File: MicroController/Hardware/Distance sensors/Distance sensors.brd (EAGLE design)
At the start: 87 x 40 mm, 37 parts, among them U1 LM2937IMP-5.0, U2 TXB0108PWR, U3 TLV1117-33CDCY, U4 TXB0108PWR, X1 0446200002, X2 0446200002, X3 0446200002

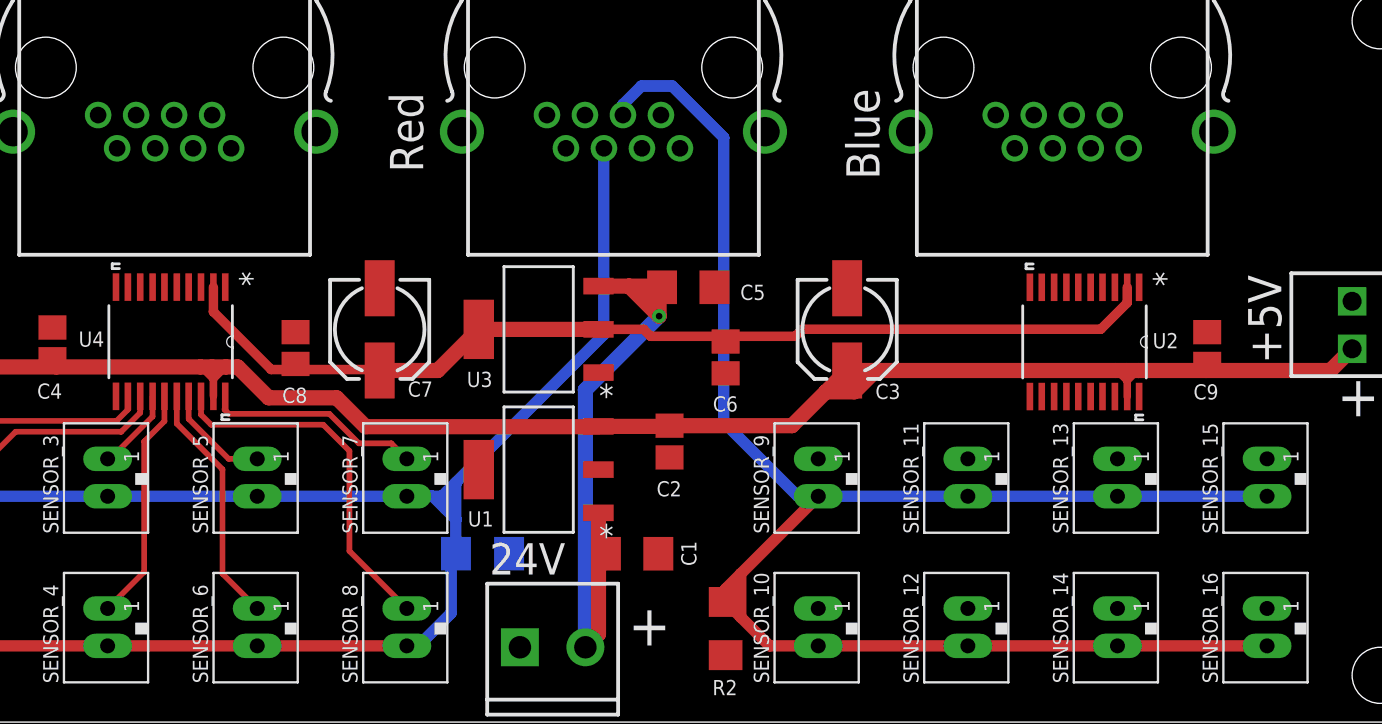
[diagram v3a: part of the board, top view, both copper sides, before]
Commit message: Version with two 5V terminals.
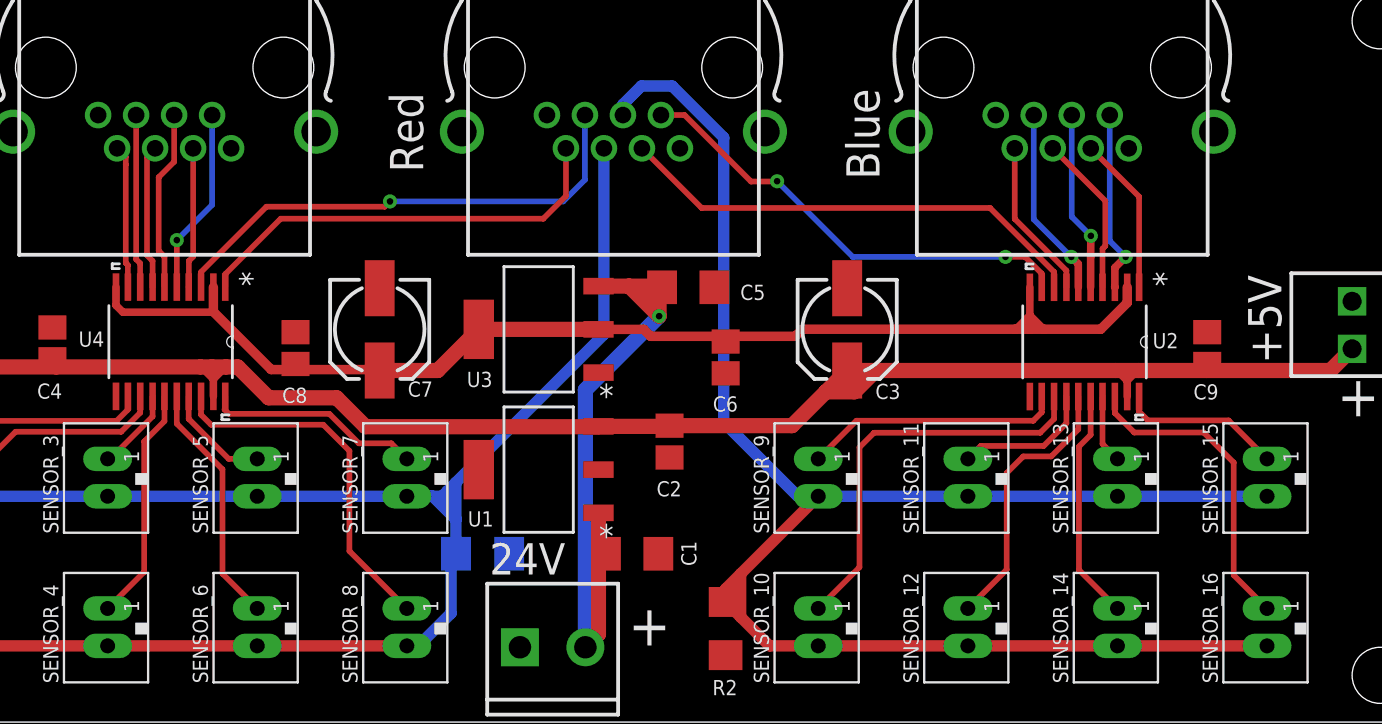
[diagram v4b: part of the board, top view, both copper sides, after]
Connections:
- removed net N$1: U4.1
- removed net N$2: U4.3
- removed net N$3: U4.4
- removed net N$4: U4.5
- removed net N$5: U4.6
- removed net N$6: U4.7
- removed net N$7: U4.8
- removed net N$8: U4.9
- net +3V3: now also U2.10, U4.10
- net ULTRA1: now also U4.9
- net ULTRA10: now also U2.8
- net ULTRA11: now also U2.7
- net ULTRA12: now also U2.6
- net ULTRA13: now also U2.4
- net ULTRA14: now also U2.5
- net ULTRA15: now also U2.1
- net ULTRA16: now also U2.3
- net ULTRA2: now also U4.8
- net ULTRA3: now also U4.7
- net ULTRA4: now also U4.6
- net ULTRA5: now also U4.4
- net ULTRA6: now also U4.5
- net ULTRA7: now also U4.1
- net ULTRA8: now also U4.3
- net ULTRA9: now also U2.9
- net ULTRAS10: now also U2.13
- net ULTRAS11: now also U2.14
- net ULTRAS12: now also U2.15
- net ULTRAS13: now also U2.17
- net ULTRAS14: now also U2.16
- net ULTRAS15: now also U2.20
- net ULTRAS16: now also U2.18
- net ULTRAS9: now also U2.12
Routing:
- net ULTRA8: track 0.00 -> 26.8 mm, vias 0 -> 1
- net ULTRA10: track 0.00 -> 25.6 mm
- net ULTRA9: track 0.00 -> 24.6 mm, vias 0 -> 2
- net ULTRA7: track 0.00 -> 23.2 mm
- net ULTRAS10: track 0.00 -> 21.8 mm
- net ULTRAS16: track 0.00 -> 16.9 mm
- net ULTRAS12: track 0.00 -> 14.7 mm
- net ULTRAS9: track 0.00 -> 13.8 mm
- net ULTRAS14: track 0.00 -> 12.4 mm
- net +3V3: track 54.9 -> 65.6 mm
- net ULTRA12: track 0.00 -> 10.2 mm, vias 0 -> 1
- net ULTRA6: track 0.00 -> 9.98 mm, vias 0 -> 1
- net ULTRA16: track 0.00 -> 9.82 mm, vias 0 -> 1
- net ULTRA4: track 0.00 -> 9.67 mm
- net ULTRA14: track 0.00 -> 9.63 mm, vias 0 -> 1
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
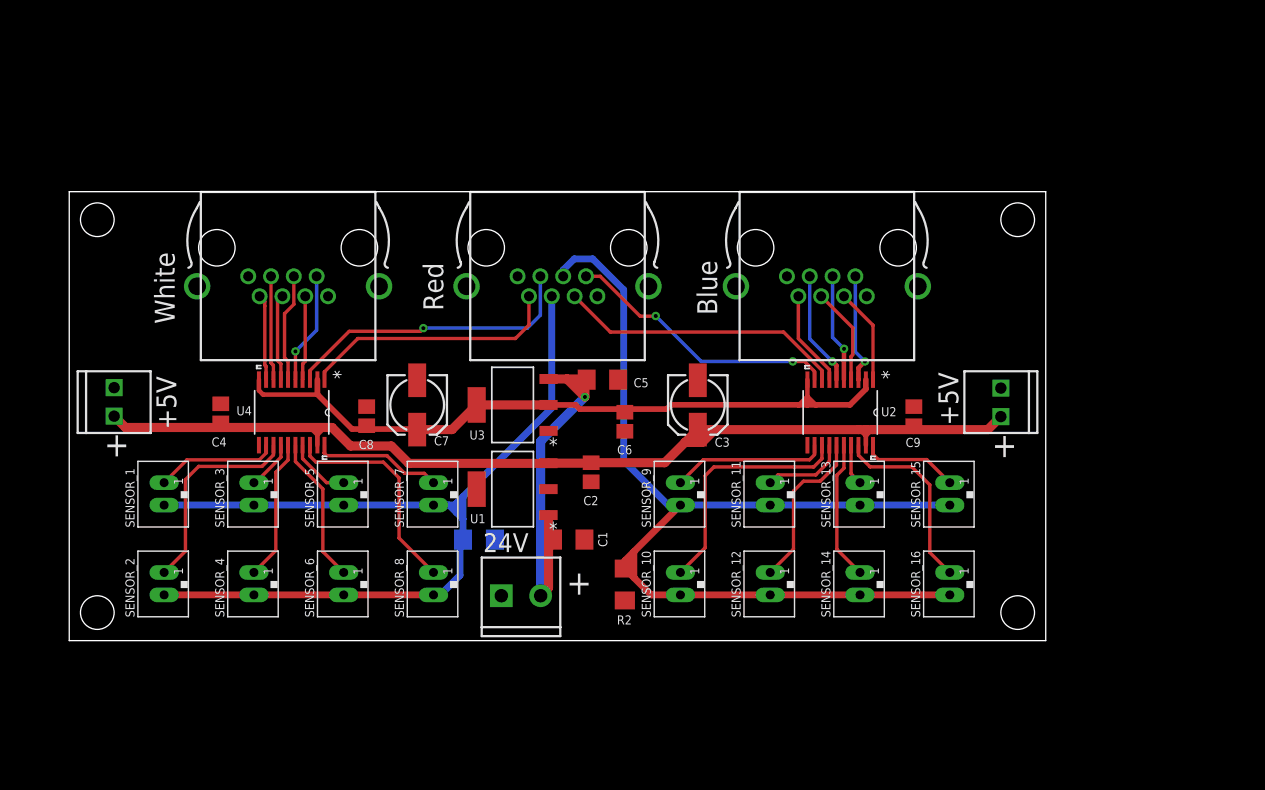
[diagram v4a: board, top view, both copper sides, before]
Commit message: Changed to one 4-pin connector for each sensor.
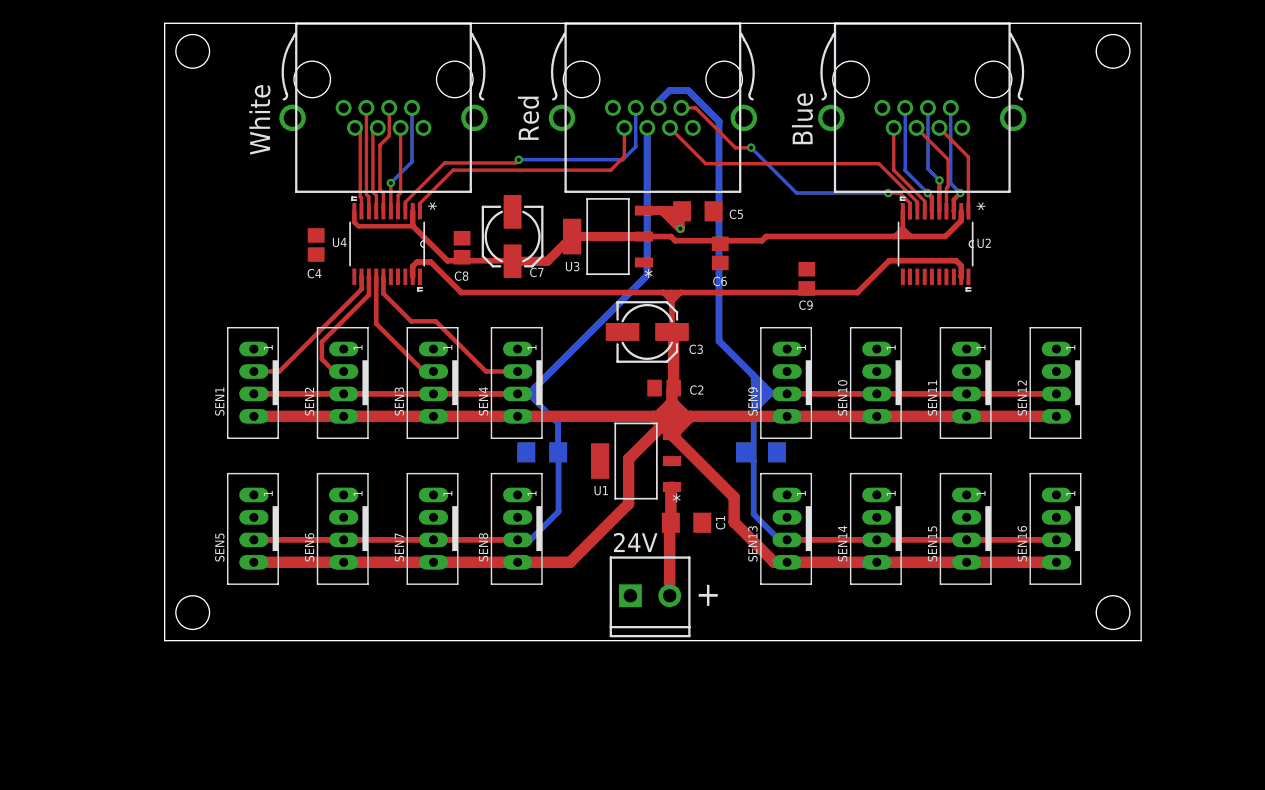
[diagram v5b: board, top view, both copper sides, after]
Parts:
- removed 5V, J1: (no value), SparkFun-Connectors:1X02_2.54_SCREWTERM
- removed SENSOR_1, SENSOR_10, SENSOR_11, SENSOR_12, SENSOR_13, SENSOR_14, SENSOR_15, SENSOR_16, SENSOR_2, SENSOR_3, SENSOR_4, SENSOR_5, SENSOR_6, SENSOR_7, SENSOR_8, SENSOR_9: JST-PH_2-PIN_HEADER, SRG:JST_B2B-PH_HEADER
- added SEN1, SEN10, SEN11, SEN12, SEN13, SEN14, SEN15, SEN16, SEN2, SEN3, SEN4, SEN5, SEN6, SEN7, SEN8, SEN9: JST-PH_4-PIN_HEADER, SRG:JST_B4B-PH_HEADER
- moved C4 17.2 mm to (13.5, 35.2)
- moved C5 17.2 mm to (47.5, 38.2)
- moved C6 17.2 mm to (49.5, 34.5)
- moved C7 17.2 mm to (31.0, 36.0)
- moved C8 17.2 mm to (26.5, 35.0)
- moved U3 17.2 mm to (39.5, 36.0)
- moved X1 17.2 mm to (19.5, 50.0)
- moved X2 17.2 mm to (43.5, 50.0)
- moved X3 17.2 mm to (67.5, 50.0)
- moved U2 17.2 mm to (68.7, 35.3)
- moved U4 17.2 mm to (19.8, 35.3)
- moved R2 16.9 mm to (53.1, 16.8), flipped to the bottom, turned to 0 degrees
- moved C9 15.5 mm to (57.2, 32.2)
- moved 24V 11.5 mm to (41.5, 4.00)
- moved U1 11.3 mm to (42.0, 16.0)
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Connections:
- net +5V: now also SEN1.P4, SEN10.P4, SEN11.P4, SEN12.P4, SEN13.P4, SEN14.P4, SEN15.P4, SEN16.P4, SEN2.P4, SEN3.P4, SEN4.P4, SEN5.P4, SEN6.P4, SEN7.P4, SEN8.P4, SEN9.P4; no longer 5V.P2, J1.P1
- net GND: now also SEN1.P1, SEN10.P1, SEN11.P1, SEN12.P1, SEN13.P1, SEN14.P1, SEN15.P1, SEN16.P1, SEN2.P1, SEN3.P1, SEN4.P1, SEN5.P1, SEN6.P1, SEN7.P1, SEN8.P1, SEN9.P1; no longer 5V.P1, J1.P2
- net TRIGGER_1: now also SEN1.P3, SEN2.P3, SEN3.P3, SEN4.P3, SEN5.P3, SEN6.P3, SEN7.P3, SEN8.P3; no longer SENSOR_1.P2, SENSOR_2.P2, SENSOR_3.P2, SENSOR_4.P2, SENSOR_5.P2, SENSOR_6.P2, SENSOR_7.P2, SENSOR_8.P2
- net TRIGGER_2: now also SEN10.P3, SEN11.P3, SEN12.P3, SEN13.P3, SEN14.P3, SEN15.P3, SEN16.P3, SEN9.P3; no longer SENSOR_10.P2, SENSOR_11.P2, SENSOR_12.P2, SENSOR_13.P2, SENSOR_14.P2, SENSOR_15.P2, SENSOR_16.P2, SENSOR_9.P2
- net ULTRAS1: now also SEN1.P2; no longer SENSOR_1.P1
- net ULTRAS10: now also SEN10.P2; no longer SENSOR_10.P1
- net ULTRAS11: now also SEN11.P2; no longer SENSOR_11.P1
- net ULTRAS12: now also SEN12.P2; no longer SENSOR_12.P1
- net ULTRAS13: now also SEN13.P2; no longer SENSOR_13.P1
- net ULTRAS14: now also SEN14.P2; no longer SENSOR_14.P1
- net ULTRAS15: now also SEN15.P2; no longer SENSOR_15.P1
- net ULTRAS16: now also SEN16.P2; no longer SENSOR_16.P1
- net ULTRAS2: now also SEN2.P2; no longer SENSOR_2.P1
- net ULTRAS3: now also SEN3.P2; no longer SENSOR_3.P1
- net ULTRAS4: now also SEN4.P2; no longer SENSOR_4.P1
- net ULTRAS5: now also SEN5.P2; no longer SENSOR_5.P1
- net ULTRAS6: now also SEN6.P2; no longer SENSOR_6.P1
- net ULTRAS7: now also SEN7.P2; no longer SENSOR_7.P1
- net ULTRAS8: now also SEN8.P2; no longer SENSOR_8.P1
- net ULTRAS9: now also SEN9.P2; no longer SENSOR_9.P1
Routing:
- net +5V: track 93.1 -> 232.6 mm
- net ULTRAS10: track 21.8 -> 0.00 mm
- net ULTRAS8: track 19.4 -> 0.00 mm
- net +24V: track 34.7 -> 17.1 mm
- net ULTRAS16: track 16.9 -> 0.00 mm
- net ULTRAS12: track 14.7 -> 0.00 mm
- net ULTRAS9: track 13.8 -> 0.00 mm
- net TRIGGER_2: track 93.4 -> 106.9 mm
- net ULTRAS6: track 13.1 -> 0.00 mm
- net ULTRAS14: track 12.4 -> 0.00 mm
- net ULTRAS7: track 11.6 -> 0.00 mm
- net ULTRAS15: track 8.69 -> 0.00 mm
- net ULTRAS11: track 7.49 -> 0.00 mm
- net ULTRAS2: track 18.7 -> 11.5 mm
- net TRIGGER_1: track 86.4 -> 93.4 mm
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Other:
- board size 87 x 40 mm -> 87 x 55 mm
- board text removed: "+5V"

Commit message: Finished the first version of the Ultrasone PCB.
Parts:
- added C10, C11, C12, C13: (no value), adafruit:C0805
- moved C4 24.2 mm to (37.1, 29.8), turned to 270 degrees
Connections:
- net +5V: now also C10.1, C11.1, C12.1, C13.1
- net GND: now also C10.2, C11.2, C12.2, C13.2
- net ULTRA13: now also U2.5; no longer U2.4
- net ULTRA14: now also U2.4; no longer U2.5
- net ULTRA15: now also U2.3; no longer U2.1
- net ULTRA16: now also U2.1; no longer U2.3
- net ULTRA5: now also U4.5; no longer U4.4
- net ULTRA6: now also U4.4; no longer U4.5
- net ULTRA7: now also U4.3; no longer U4.1
- net ULTRA8: now also U4.1; no longer U4.3
- net ULTRAS13: now also U2.16; no longer U2.17
- net ULTRAS14: now also U2.17; no longer U2.16
- net ULTRAS15: now also U2.18; no longer U2.20
- net ULTRAS16: now also U2.20; no longer U2.18
- net ULTRAS5: now also U4.16; no longer U4.17
- net ULTRAS6: now also U4.17; no longer U4.16
- net ULTRAS7: now also U4.18; no longer U4.20
- net ULTRAS8: now also U4.20; no longer U4.18
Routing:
- net +24V: track 17.1 -> 50.2 mm
- net ULTRAS13: track 0.00 -> 28.9 mm, vias 0 -> 1
- net ULTRAS5: track 0.00 -> 28.0 mm, vias 0 -> 1
- net ULTRAS8: track 0.00 -> 26.2 mm, vias 0 -> 1
- net ULTRAS16: track 0.00 -> 25.8 mm, vias 0 -> 1
- net ULTRAS7: track 0.00 -> 25.7 mm, vias 0 -> 1
- net ULTRAS15: track 0.00 -> 25.4 mm, vias 0 -> 1
- net ULTRAS6: track 0.00 -> 25.0 mm, vias 0 -> 1
- net ULTRAS14: track 0.00 -> 24.9 mm, vias 0 -> 1
- net ULTRAS12: track 0.00 -> 16.2 mm
- net ULTRAS9: track 0.00 -> 15.0 mm
- net ULTRAS11: track 0.00 -> 10.4 mm
- net ULTRAS10: track 0.00 -> 10.1 mm
- net +5V: track 232.6 -> 238.0 mm
- net ULTRA8: track 26.8 -> 25.3 mm, vias 1 -> 0
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- added copper zone on layer 1, net GND
- added copper zone on layer 16, net GND
